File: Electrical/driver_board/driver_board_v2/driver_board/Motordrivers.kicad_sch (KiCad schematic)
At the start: 24 parts

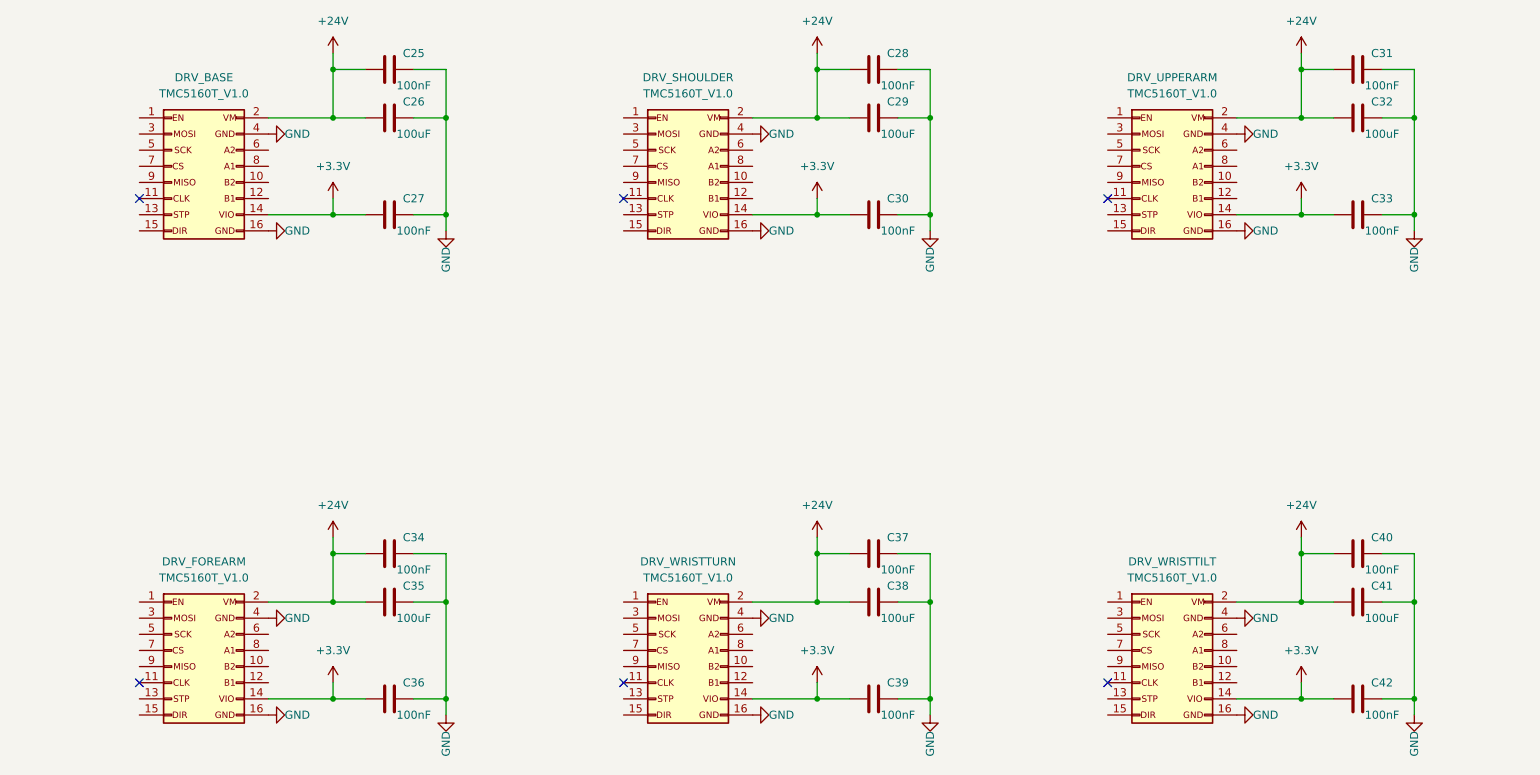
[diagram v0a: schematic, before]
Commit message: Added gripper
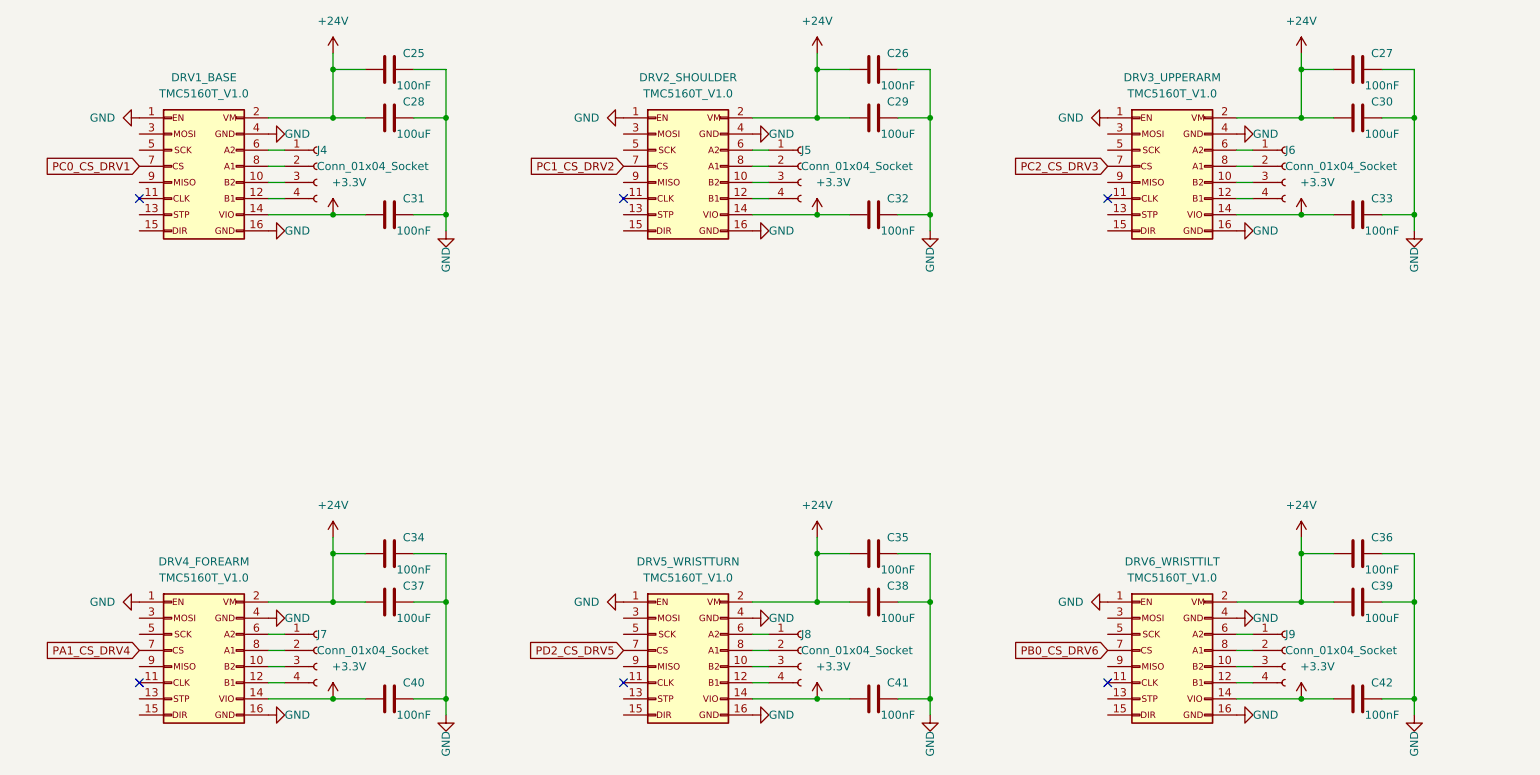
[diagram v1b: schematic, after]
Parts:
- added J4, J5, J6, J7, J8, J9: Conn_01x04_Socket, Connector_JST:JST_XH_B4B-XH-A_1x04_P2.50mm_Vertical, symbol Connector:Conn_01x04_Socket
- C35, C41: value 100uF -> 100nF
- C37, C39: value 100nF -> 100uF
- renumbered C28 to C26, C31 to C27, C26 to C28, C32 to C30, C27 to C31, C30 to C32, DRV_BASE to DRV1_BASE, DRV_SHOULDER to DRV2_SHOULDER, DRV_UPPERARM to DRV3_UPPERARM, DRV_FOREARM to DRV4_FOREARM, DRV_WRISTTURN to DRV5_WRISTTURN, DRV_WRISTTILT to DRV6_WRISTTILT
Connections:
- net +24V: now also C36.1, C39.1; no longer C40.1, C41.1
- net +3.3V: now also C40.1, C41.1; no longer C36.1, C39.1
- net GND: now also DRV1_BASE.1 (Pin_1), DRV2_SHOULDER.1 (Pin_1), DRV3_UPPERARM.1 (Pin_1), DRV4_FOREARM.1 (Pin_1), DRV5_WRISTTURN.1 (Pin_1), DRV6_WRISTTILT.1 (Pin_1)
- net at DRV2_SHOULDER.10 (Pin_10): now also J5.3 (Pin_3)
- net at DRV2_SHOULDER.12 (Pin_12): now also J5.4 (Pin_4)
- net at DRV2_SHOULDER.6 (Pin_6): now also J5.1 (Pin_1)
- net PC1_CS_DRV2: now reaches DRV2_SHOULDER.7 (Pin_7)
- net at DRV2_SHOULDER.8 (Pin_8): now also J5.2 (Pin_2)
- net at DRV4_FOREARM.10 (Pin_10): now also J7.3 (Pin_3)
- net at DRV4_FOREARM.12 (Pin_12): now also J7.4 (Pin_4)
- net at DRV4_FOREARM.6 (Pin_6): now also J7.1 (Pin_1)
- net PA1_CS_DRV4: now reaches DRV4_FOREARM.7 (Pin_7)
- net at DRV4_FOREARM.8 (Pin_8): now also J7.2 (Pin_2)
- net at DRV3_UPPERARM.10 (Pin_10): now also J6.3 (Pin_3)
- net at DRV3_UPPERARM.12 (Pin_12): now also J6.4 (Pin_4)
- net at DRV3_UPPERARM.6 (Pin_6): now also J6.1 (Pin_1)
- net PC2_CS_DRV3: now reaches DRV3_UPPERARM.7 (Pin_7)
- net at DRV3_UPPERARM.8 (Pin_8): now also J6.2 (Pin_2)
- net at DRV5_WRISTTURN.10 (Pin_10): now also J8.3 (Pin_3)
- net at DRV5_WRISTTURN.12 (Pin_12): now also J8.4 (Pin_4)
- net at DRV5_WRISTTURN.6 (Pin_6): now also J8.1 (Pin_1)
- net PD2_CS_DRV5: now reaches DRV5_WRISTTURN.7 (Pin_7)
- net at DRV5_WRISTTURN.8 (Pin_8): now also J8.2 (Pin_2)
- net at DRV6_WRISTTILT.10 (Pin_10): now also J9.3 (Pin_3)
- net at DRV6_WRISTTILT.12 (Pin_12): now also J9.4 (Pin_4)
- net at DRV6_WRISTTILT.6 (Pin_6): now also J9.1 (Pin_1)
- net PB0_CS_DRV6: now reaches DRV6_WRISTTILT.7 (Pin_7)
- net at DRV6_WRISTTILT.8 (Pin_8): now also J9.2 (Pin_2)
- net at DRV1_BASE.10 (Pin_10): now also J4.3 (Pin_3)
- net at DRV1_BASE.12 (Pin_12): now also J4.4 (Pin_4)
- net at DRV1_BASE.6 (Pin_6): now also J4.1 (Pin_1)
- net PC0_CS_DRV1: now reaches DRV1_BASE.7 (Pin_7)
- net at DRV1_BASE.8 (Pin_8): now also J4.2 (Pin_2)

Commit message: Added TMC and MCU Labeling
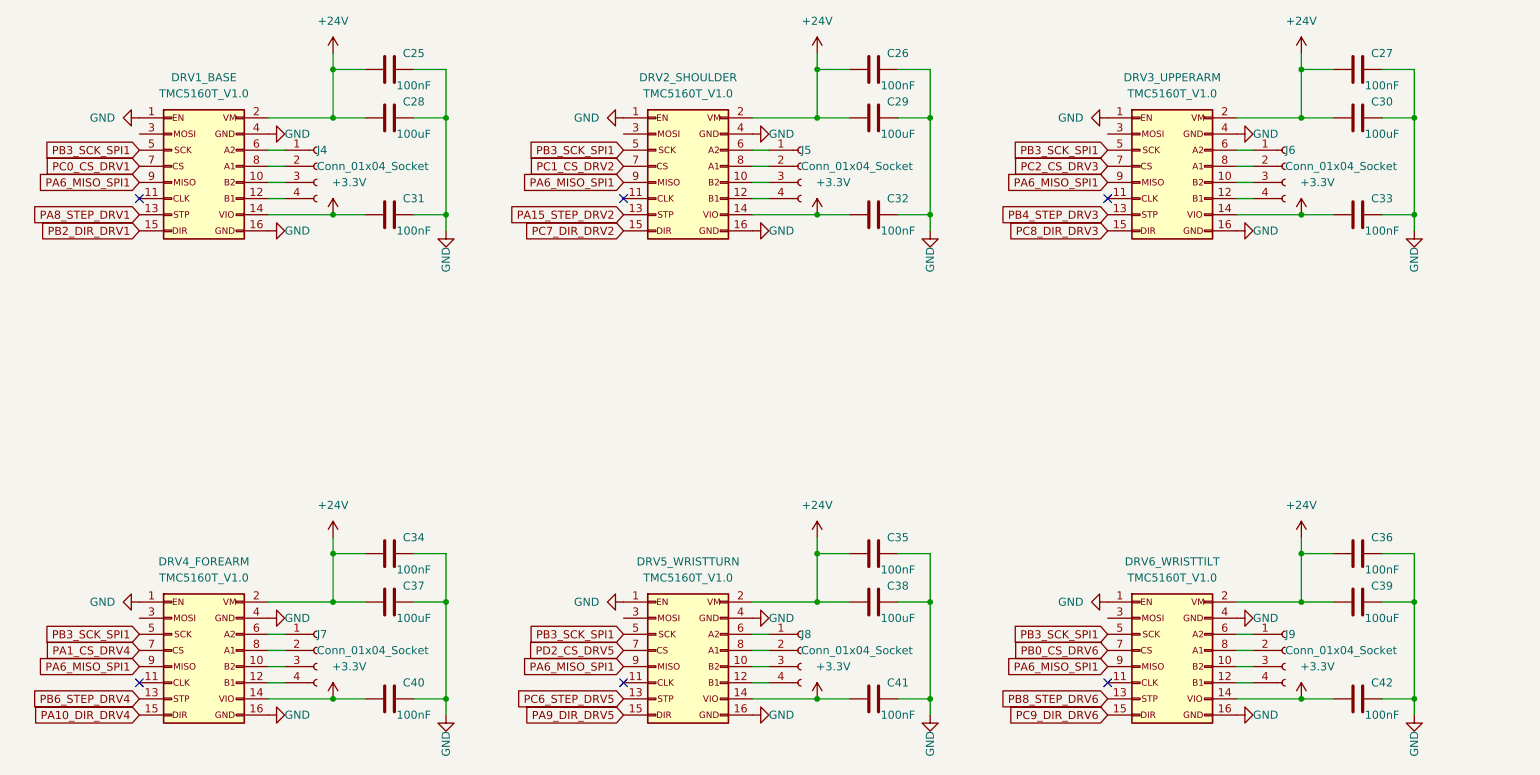
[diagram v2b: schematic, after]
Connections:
- net PA15_STEP_DRV2: now reaches DRV2_SHOULDER.13 (Pin_13)
- net PC7_DIR_DRV2: now reaches DRV2_SHOULDER.15 (Pin_15)
- net PB3_SCK_SPI1: now reaches DRV2_SHOULDER.5 (Pin_5)
- net PB3_SCK_SPI1: now also DRV1_BASE.5 (Pin_5), DRV3_UPPERARM.5 (Pin_5), DRV4_FOREARM.5 (Pin_5), DRV5_WRISTTURN.5 (Pin_5), DRV6_WRISTTILT.5 (Pin_5)
- net PA6_MISO_SPI1: now reaches DRV2_SHOULDER.9 (Pin_9)
- net PA6_MISO_SPI1: now also DRV1_BASE.9 (Pin_9), DRV3_UPPERARM.9 (Pin_9), DRV4_FOREARM.9 (Pin_9), DRV5_WRISTTURN.9 (Pin_9), DRV6_WRISTTILT.9 (Pin_9)
- net PB6_STEP_DRV4: now reaches DRV4_FOREARM.13 (Pin_13)
- net PA10_DIR_DRV4: now reaches DRV4_FOREARM.15 (Pin_15)
- net PB4_STEP_DRV3: now reaches DRV3_UPPERARM.13 (Pin_13)
- net PC8_DIR_DRV3: now reaches DRV3_UPPERARM.15 (Pin_15)
- net PC6_STEP_DRV5: now reaches DRV5_WRISTTURN.13 (Pin_13)
- net PA9_DIR_DRV5: now reaches DRV5_WRISTTURN.15 (Pin_15)
- net PB8_STEP_DRV6: now reaches DRV6_WRISTTILT.13 (Pin_13)
- net PC9_DIR_DRV6: now reaches DRV6_WRISTTILT.15 (Pin_15)
- net PA8_STEP_DRV1: now reaches DRV1_BASE.13 (Pin_13)
- net PB2_DIR_DRV1: now reaches DRV1_BASE.15 (Pin_15)

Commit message: Finished TMC Labeling
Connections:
- net PB5_MOSI_SPI1: now reaches DRV2_SHOULDER.3 (Pin_3)
- net PB5_MOSI_SPI1: now also DRV1_BASE.3 (Pin_3), DRV3_UPPERARM.3 (Pin_3), DRV4_FOREARM.3 (Pin_3), DRV5_WRISTTURN.3 (Pin_3), DRV6_WRISTTILT.3 (Pin_3)
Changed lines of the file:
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@@
+		)
+	)
+	(global_label "PB5_MOSI_SPI1"
+		(shape input)
+		(at 40.64 121.92 180)
+		(fields_autoplaced yes)
+		(effects
+			(font
+				(size 1.27 1.27)
+			)
+			(justify right)
+		)
+		(property "Intersheetrefs" "${INTERSHEET_REFS}"
+			(at 23.0801 121.92 0)
+			(effects
+				(font
+					(size 1.27 1.27)
+				)
+				(justify right)
+				(hide yes)
+			)
 		)
 	)
@@
 		)
 	)
+	(global_label "PB5_MOSI_SPI1"
+		(shape input)
+		(at 193.04 45.72 180)
+		(fields_autoplaced yes)
+		(effects
+			(font
+				(size 1.27 1.27)
+			)
+			(justify right)
+		)
+		(property "Intersheetrefs" "${INTERSHEET_REFS}"
+			(at 175.4801 45.72 0)
+			(effects
+				(font
+					(size 1.27 1.27)
+				)
+				(justify right)
+				(hide yes)
+			)
+		)
+	)
 	(global_label "PB2_DIR_DRV1"
 		(shape input)
@@
 		)
 	)
+	(global_label "PB5_MOSI_SPI1"
+		(shape input)
+		(at 40.64 45.72 180)
+		(fields_autoplaced yes)
+		(effects
+			(font
+				(size 1.27 1.27)
+			)
+			(justify right)
+		)
+		(property "Intersheetrefs" "${INTERSHEET_REFS}"
+			(at 23.0801 45.72 0)
+			(effects
+				(font
+					(size 1.27 1.27)
+				)
+				(justify right)
+				(hide yes)
+			)
+		)
+	)
 	(global_label "PC0_CS_DRV1"
 		(shape input)
@@
 		)
 	)
+	(global_label "PB5_MOSI_SPI1"
+		(shape input)
+		(at 116.84 45.72 180)
+		(fields_autoplaced yes)
+		(effects
+			(font
+				(size 1.27 1.27)
+			)
+			(justify right)
+		)
+		(property "Intersheetrefs" "${INTERSHEET_REFS}"
+			(at 99.2801 45.72 0)
+			(effects
+				(font
+					(size 1.27 1.27)
+				)
+				(justify right)
+				(hide yes)
+			)
+		)
+	)
 	(global_label "PB8_STEP_DRV6"
 		(shape input)
@@
 		)
 	)
+	(global_label "PB5_MOSI_SPI1"
+		(shape input)
+		(at 193.04 121.92 180)
+		(fields_autoplaced yes)
+		(effects
+			(font
+				(size 1.27 1.27)
+			)
+			(justify right)
+		)
+		(property "Intersheetrefs" "${INTERSHEET_REFS}"
+			(at 175.4801 121.92 0)
+			(effects
+				(font
+					(size 1.27 1.27)
+				)
+				(justify right)
+				(hide yes)
+			)
+		)
+	)
 	(global_label "PC6_STEP_DRV5"
 		(shape input)
@@
 			(effects
 				(font
+					(size 1.27 1.27)
+				)
+				(justify right)
+				(hide yes)
+			)
+		)
+	)
+	(global_label "PB5_MOSI_SPI1"
+		(shape input)
+		(at 116.84 121.92 180)
+		(fields_autoplaced yes)
+		(effects
+			(font
+				(size 1.27 1.27)
+			)
+			(justify right)
+		)
+		(property "Intersheetrefs" "${INTERSHEET_REFS}"
+			(at 99.2801 121.92 0)
+			(effects
+				(font

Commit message: Added gnd plane
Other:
- note added: "Motordrivers"
- moved on the sheet: C25, C26, C27, C28, C29, C30, C31, C32, C33, C34, C35, C36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
